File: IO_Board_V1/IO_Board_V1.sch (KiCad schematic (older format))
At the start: 92 parts, among them J1 USB_C_Receptacle_USB2.0, J10 IFM1, J11 FOURCHE, J12 BTN, J13 FOURCHE, J14 BTN, J15 CON_UART, J16 BTN, J17 FOURCHE, J18 IFM2, J19 IFM3, J2 CON_debug, J20 FOURCHE, J21 CON_I2C, J22 IFM4, J23 SPI, J24 BTN, J3 Conn_ARM_JTAG_SWD_10, J4 CON_CAN, J5 CON_CAN, J6 12V, J7 BTN, J8 BTN, J9 IFM0, SW1 BOOT, SW2 RST, U1 STM32F302C6Tx, U2 NCP1117-3.3_SOT223, U3 SN65HVD232, Y1 8MHz

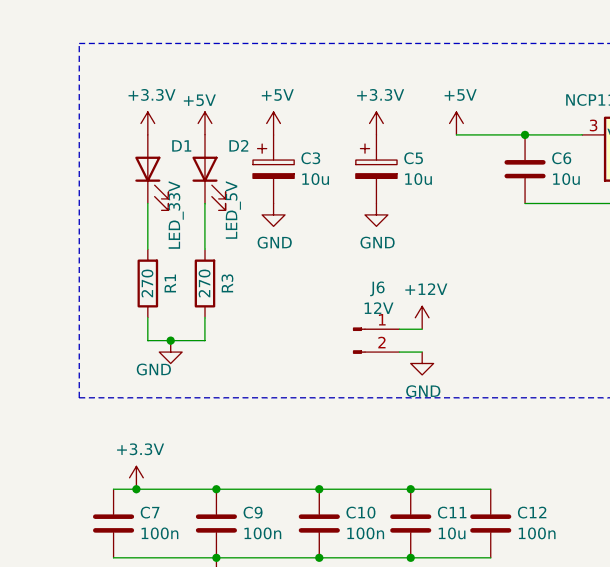
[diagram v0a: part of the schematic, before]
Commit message: IO prete, Pompe finir sérigraphie, Alim+AX12 à faire
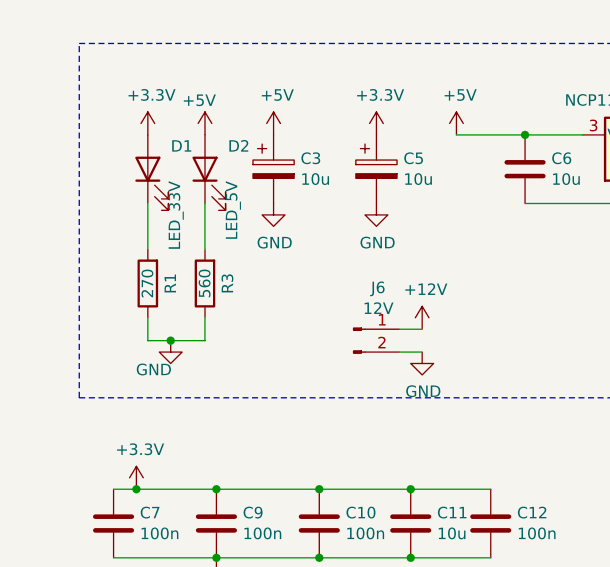
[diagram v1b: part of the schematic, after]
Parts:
- R3: value 270 -> 560
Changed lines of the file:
@@
 P 1250 1750
 F 0 "R3" V 1150 1750 50  0000 C CNN
-F 1 "270" V 1250 1750 50  0000 C CNN
+F 1 "560" V 1250 1750 50  0000 C CNN
 F 2 "Resistor_SMD:R_0805_2012Metric" V 1180 1750 50  0001 C CNN
 F 3 "~" H 1250 1750 50  0001 C CNN
